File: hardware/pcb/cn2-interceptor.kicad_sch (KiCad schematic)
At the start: 6 parts, among them J1 JST-XH 4P CONTROLLER CN2, J2 JST-XH 4P PANEL CN2, J3 JST-XH 3P FLOW METER, J4 JST-XH 3P FV TO CONTROLLER, U1 XIAO ESP32-C3, U2 4CH BSS138 LEVEL SHIFTER

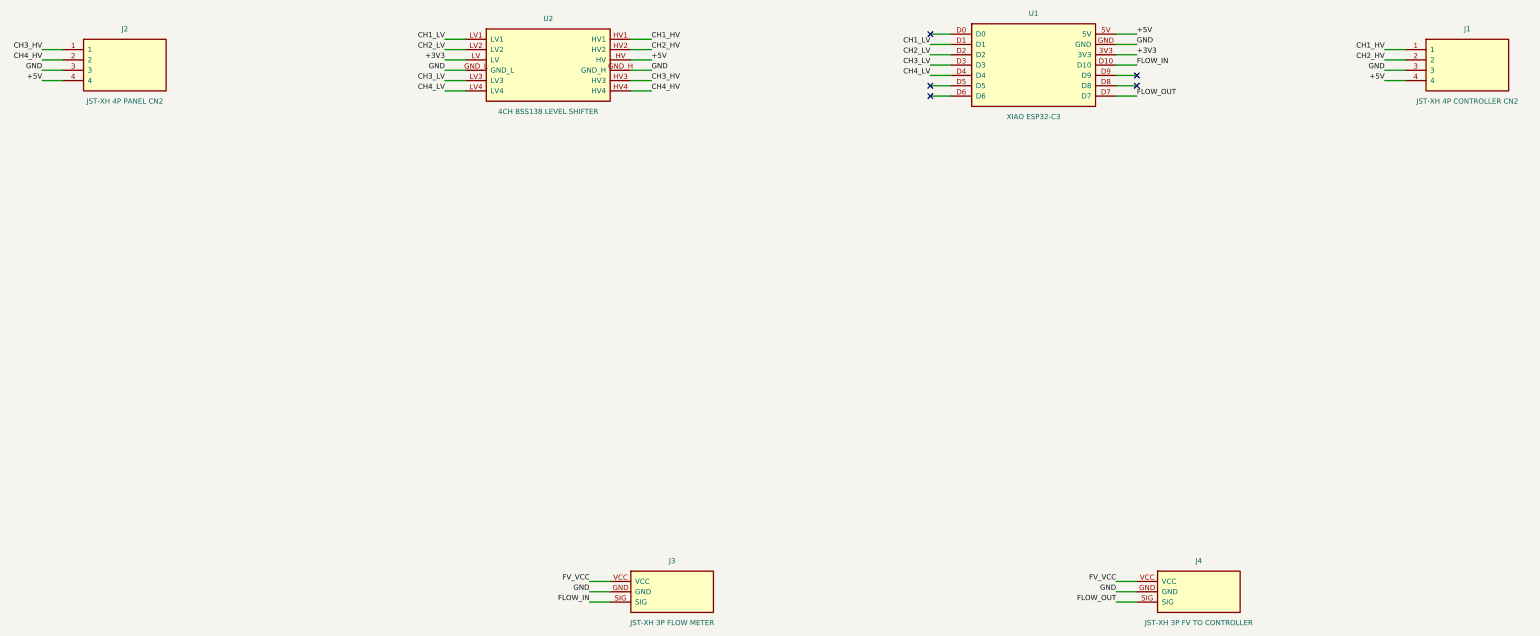
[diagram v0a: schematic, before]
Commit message: pcb: 18.6 x 27 mm — connectors on opposite edges, flow relay dropped
39% less area and 41% narrower than the 31.5 x 26 board, which is the
dimension that decides whether it fits inside the appliance. Nothing about
the CN2 interception changes.

What made it small: the XIAO's two pad rows are 15.24 mm apart, so anything
standing beside them adds width directly, and the old board had a connector
on each side. Moving both to the top and bottom edges leaves nothing outside
the module except one routing lane -- shared by +5V on top and GND on the
bottom -- so the width is now pad block + lane + two edges, fully accounted
for and with nothing left in it. Each CN2 signal pin sits directly under the
middle corridor and climbs straight out of its own pad into its shifter pin,
turning once, so the four signals need no side lane at all.

The flow-meter relay (J3/J4) is gone, per Kai's call. Its six pins could not
share an edge with the CN2 connectors, so they were what forced the
connectors back onto the sides: that one feature cost more board than
everything else on it. The two hard-won warnings about it (the C3 is not 5 V
tolerant with no channel left to shift FV, and cutting the line strands the
meter's pull-up on the far side) are kept in the README for whoever re-adds
it.

Which connector goes on which edge is load-bearing, not cosmetic. Routing
forces LV1..LV4 onto D1..D4 in order -- they share a 0.94 mm channel and any
other order overlaps four deep -- and D1..D4 are GPIO3,4,5,6. The firmware's
as-built map puts the controller on GPIO5/6, which are the shifter's upper
channels, so the controller enters from the top. Get it backwards and the
board still works but only after swapping four defines, and a pin map that
disagrees with the copper does not announce itself: frames just stop
decoding. gen_pcb.py now reads firmware/include/config.h and fails on a
mismatch rather than leaving that to a comment.

Two new checks, both of which caught something real:

  MECHANICAL  th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
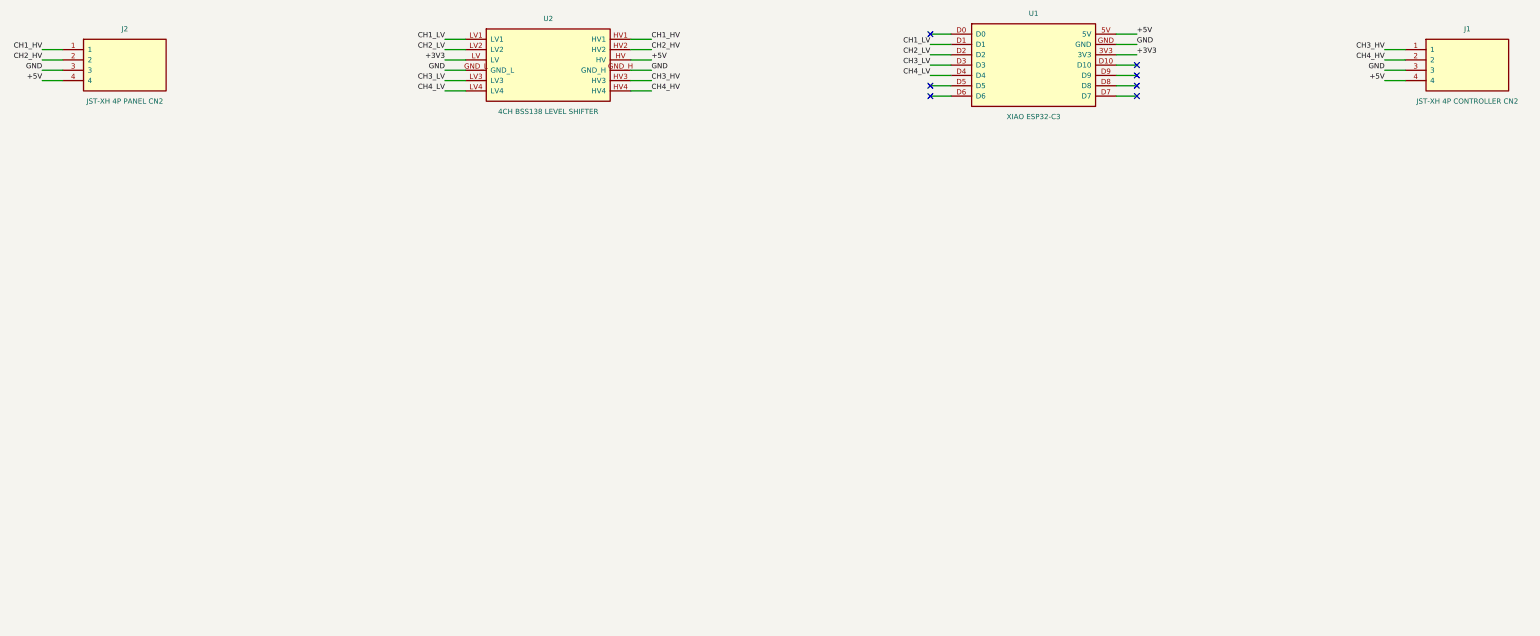
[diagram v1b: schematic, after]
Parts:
- removed J3: JST-XH 3P FLOW METER, symbol cn2:J3_SYM
- removed J4: JST-XH 3P FV TO CONTROLLER, symbol cn2:J4_SYM
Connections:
- net CH1_HV: now also J2.1; no longer J1.1
- net CH2_HV: now also J2.2; no longer J1.2
- net CH3_HV: now also J1.1; no longer J2.1
- net CH4_HV: now also J1.2; no longer J2.2
- net FLOW_IN: no longer names the net of U1.D10
- net FLOW_OUT: no longer names the net of U1.D7
- no-connect marks 5 -> 7
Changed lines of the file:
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@@
   (wire (pts (xy 53.34 118.11) (xy 48.26 118.11))
     (stroke (width 0) (type default)))
-  (label "CH3_HV" (at 48.26 118.11 0) (effects (font (size 1.27 1.27)) (justify right bottom)))
+  (label "CH1_HV" (at 48.26 118.11 0) (effects (font (size 1.27 1.27)) (justify right bottom)))
   (wire (pts (xy 53.34 120.65) (xy 48.26 120.65))
     (stroke (width 0) (type default)))
-  (label "CH4_HV" (at 48.26 120.65 0) (effects (font (size 1.27 1.27)) (justify right bottom)))
+  (label "CH2_HV" (at 48.26 120.65 0) (effects (font (size 1.27 1.27)) (justify right bottom)))
   (wire (pts (xy 53.34 123.19) (xy 48.26 123.19))
     (stroke (width 0) (type default)))
@@
   (wire (pts (xy 312.42 121.92) (xy 317.50 121.92))
     (stroke (width 0) (type default)))
-  (label "FLOW_IN" (at 317.50 121.92 0) (effects (font (size 1.27 1.27)) (justify left bottom)))
+  (no_connect (at 317.50 121.92))
   (wire (pts (xy 312.42 124.46) (xy 317.50 124.46))
     (stroke (width 0) (type default)))
@@
   (wire (pts (xy 312.42 129.54) (xy 317.50 129.54))
     (stroke (width 0) (type default)))
-  (label "FLOW_OUT" (at 317.50 129.54 0) (effects (font (size 1.27 1.27)) (justify left bottom)))
+  (no_connect (at 317.50 129.54))
   (symbol (lib_id "cn2:J1_SYM") (at 398.78 121.92 0) (unit 1)
     (in_bom yes) (on_board yes) (dnp no)
@@
   (wire (pts (xy 383.54 118.11) (xy 378.46 118.11))
     (stroke (width 0) (type default)))
-  (label "CH1_HV" (at 378.46 118.11 0) (effects (font (size 1.27 1.27)) (justify right bottom)))
+  (label "CH3_HV" (at 378.46 118.11 0) (effects (font (size 1.27 1.27)) (justify right bottom)))
   (wire (pts (xy 383.54 120.65) (xy 378.46 120.65))
     (stroke (width 0) (type default)))
-  (label "CH2_HV" (at 378.46 120.65 0) (effects (font (size 1.27 1.27)) (justify right bottom)))
+  (label "CH4_HV" (at 378.46 120.65 0) (effects (font (size 1.27 1.27)) (justify right bottom)))
   (wire (pts (xy 383.54 123.19) (xy 378.46 123.19))
     (stroke (width 0) (type default)))
@@
     (stroke (width 0) (type default)))
   (label "+5V" (at 378.46 125.73 0) (effects (font (size 1.27 1.27)) (justify right bottom)))
-  (symbol (lib_id "cn2:J3_SYM") (at 203.20 251.46 0) (unit 1)
-    (in_bom yes) (on_board yes) (dnp no)
-    (property "Reference" "J3" (at 203.20 243.84 0) (effects (font (size 1.27 1.27))))
-    (property "Value" "JST-XH 3P  FLOW METER" (at 203.20 259.08 0) (effects (font (size 1.27 1.27))))
-    (property "Footprint" "" (at 203.20 251.46 0) (effects (font (size 1.27 1.27)) hide))
-    (property "Datasheet" "" (at 203.20 251.46 0) (effects (font (size 1.27 1.27)) hide))
-    (pin "VCC")
-    (pin "GND")
-    (pin "SIG")
-    (instances (project "cn2-interceptor"
-      (path "/00000000-0000-0000-0000-000000000108" (reference "J3") (unit 1))))
-  )
-  (wire (pts (xy 187.96 248.92) (xy 182.88 248.92))
-    (stroke (width 0) (type default)))
-  (label "FV_VCC" (at 182.88 248.92 0) (effects (font (size 1.27 1.27)) (justify right bottom)))
-  (wire (pts (xy 187.96 251.46) (xy 182.88 251.46))
-    (stroke (width 0) (type default)))
-  (label "GND" (at 182.88 251.46 0) (effects (font (size 1.27 1.27)) (justify right bottom)))
-  (wire (pts (xy 187.96 254.00) (xy 182.88 254.00))
-    (stroke (width 0) (type default)))
-  (label "FLOW_IN" (at 182.88 254.00 0) (effects (font (size 1.27 1.27)) (justify right bottom)))
-  (symbol (lib_id "cn2:J4_SYM") (at 332.74 251.46 0) (unit 1)
-    (in_bom yes) (on_board yes) (dnp no)
-    (property "Reference" "J4" (at 332.74 243.84 0) (effects (font (size 1.27 1.27))))
-    (property "Value" "JST-XH 3P  FV TO CONTROLLER" (at 332.74 259.08 0) (effects (font (size 1.27 1.27))))
-    (property "Footprint" "" (at 332.74 251.46 0) (effects (font (size 1.27 1.27)) hide))
-    (property "Datasheet" "" (at 332.74 251.46 0) (effects (font (size 1.27 1.27)) hide))
-    (pin "VCC")
-    (pin "GND")
-    (pin "SIG")
-    (instances (project "cn2-interceptor"
-      (path "/00000000-0000-0000-0000-000000000118" (reference "J4") (unit 1))))
-  )
-  (wire (pts (xy 317.50 248.92) (xy 312.42 248.92))
-    (stroke (width 0) (type default)))
-  (label "FV_VCC" (at 312.42 248.92 0) (effects (font (size 1.27 1.27)) (justify right bottom)))
-  (wire (pts (xy 317.50 251.46) (xy 312.42 251.46))
-    (stroke (width 0) (type default)))
-  (label "GND" (at 312.42 251.46 0) (effects (font (size 1.27 1.27)) (justify right bottom)))
-  (wire (pts (xy 317.50 254.00) (xy 312.42 254.00))
-    (stroke (width 0) (type default)))
-  (label "FLOW_OUT" (at 312.42 254.00 0) (effects (font (size 1.27 1.27)) (justify right bottom)))
   (sheet_instances (path "/" (page "1")))
 )
